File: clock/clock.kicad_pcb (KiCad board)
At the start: 2 copper layers, 100 x 50 mm, 165 parts, among them J1 Conn_02x05_Odd_Even, P1 Conn_WallPlug, U1 74HC596, U10 74HC596, U11 LPC804-TSSOP24, U2 74HC596, U3 74HC596, U4 74HC596, U5 74HC596, U6 74HC596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

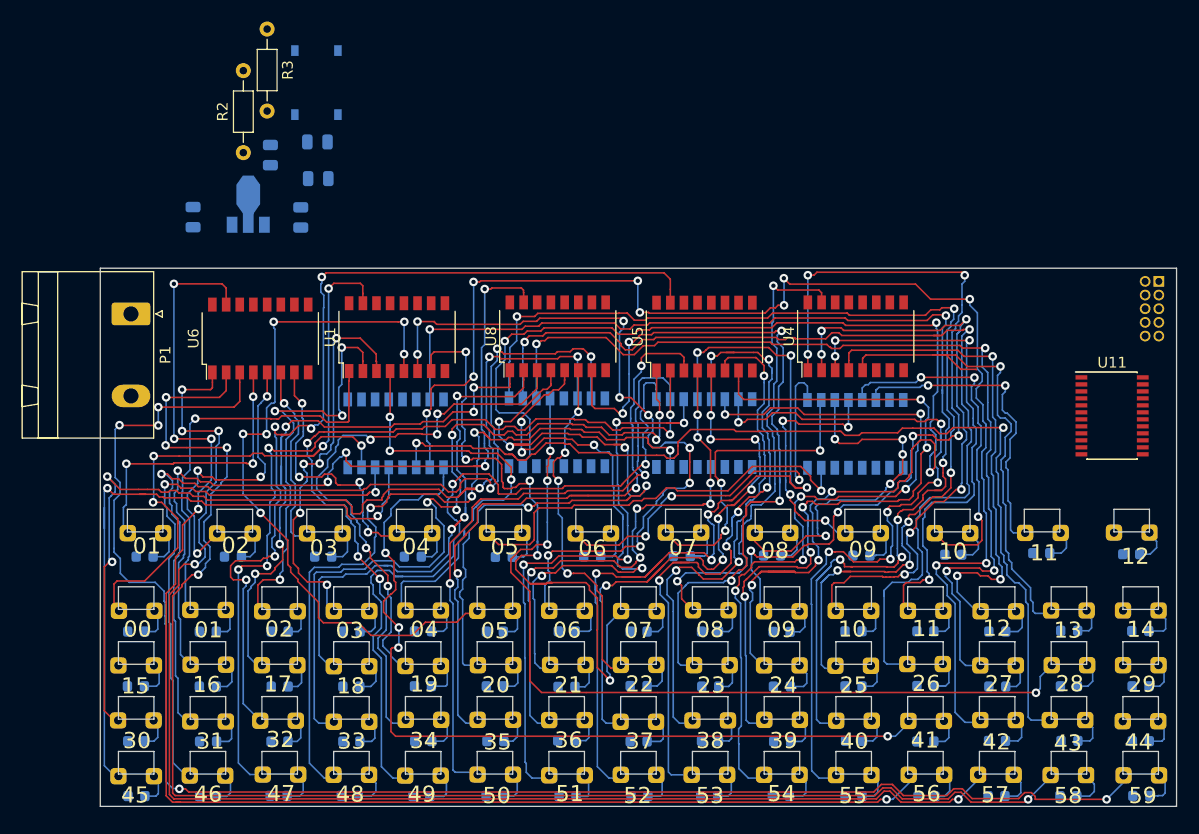
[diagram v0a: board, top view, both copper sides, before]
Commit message: All LEDs routed. Will consider some optimization e.g. via reduction or shorting traces.
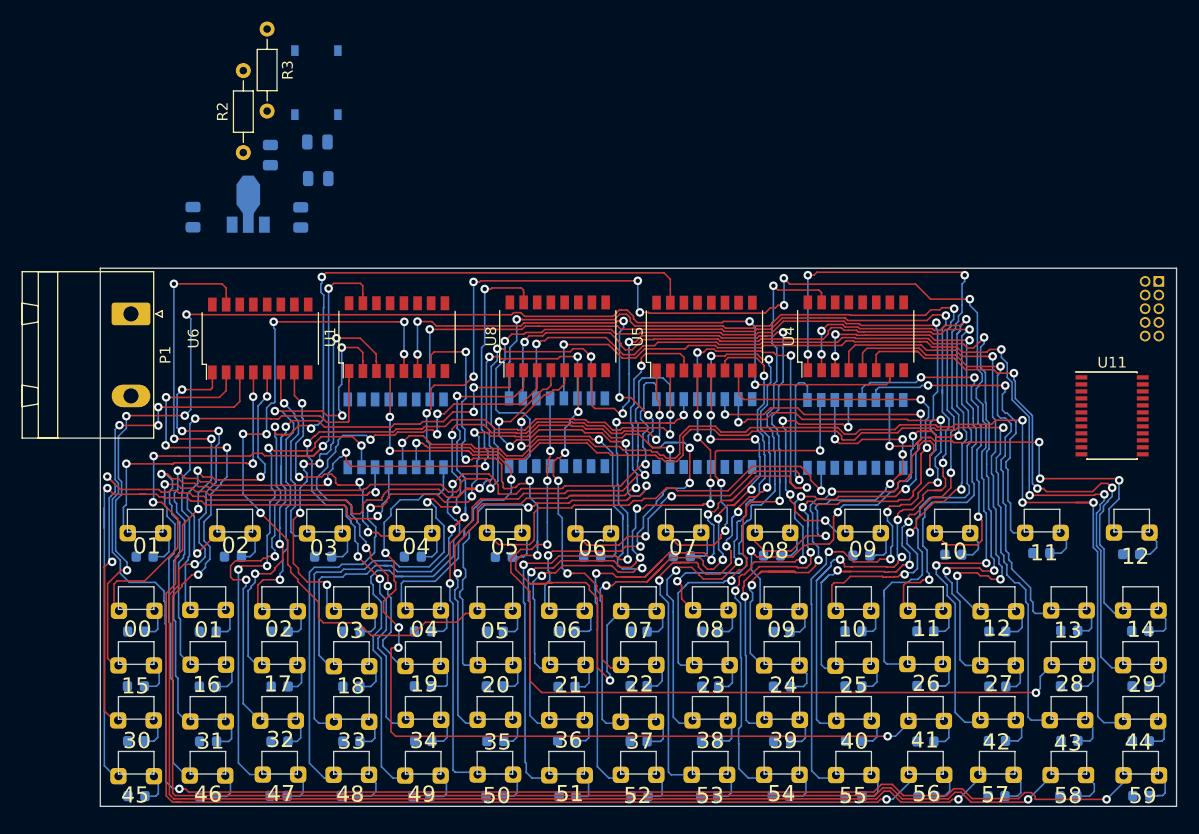
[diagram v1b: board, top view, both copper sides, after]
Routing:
- net M15: track 0.00 -> 114.5 mm, vias 0 -> 6
- net M44: track 0.00 -> 104.6 mm, vias 0 -> 4
- net M29: track 0.00 -> 87.3 mm, vias 0 -> 4
- net M14: track 0.00 -> 48.4 mm, vias 0 -> 3
- net H12: track 0.00 -> 36.1 mm, vias 0 -> 4
- net M13: track 46.3 -> 42.3 mm
- net M20: track 66.8 -> 64.5 mm
- net M27: track 85.4 -> 86.9 mm
- net M51: track 55.4 -> 54.0 mm
- net M53: track 68.7 -> 67.3 mm
- net M23: track 71.7 -> 72.7 mm
- net M48: track 72.4 -> 71.5 mm
- net M11: track 47.9 -> 48.8 mm
- net M21: track 53.8 -> 53.1 mm
- net M09: track 73.6 -> 74.3 mm

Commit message: Moving to a new work.
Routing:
- net M23: track 72.7 -> 75.4 mm
- net M24: track 116.4 -> 115.7 mm

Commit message: Added Renders
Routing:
- net M01: track 38.7 -> 45.7 mm
- net M24: track 115.7 -> 110.4 mm
- net M32: track 88.3 -> 84.9 mm
- net M30: track 91.9 -> 89.8 mm
- net M00: track 59.3 -> 60.8 mm
- net H12: track 36.1 -> 35.0 mm
- net M09: track 74.3 -> 73.2 mm
- net M25: track 97.0 -> 96.2 mm
- net M19: track 51.1 -> 50.4 mm
- net H02: track 28.2 -> 27.4 mm
- net M38: track 48.7 -> 48.1 mm
- net M43: track 93.0 -> 92.4 mm
- net M46: track 51.5 -> 50.9 mm
- net M45: track 61.8 -> 61.3 mm
- net M16: track 73.7 -> 73.1 mm
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
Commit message: saving progress
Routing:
- net M55: track 69.5 -> 68.0 mm
- net M40: track 110.9 -> 109.7 mm
- net M25: track 96.2 -> 95.2 mm
- net H11: track 29.0 -> 29.5 mm
- net M24: track 110.4 -> 109.9 mm

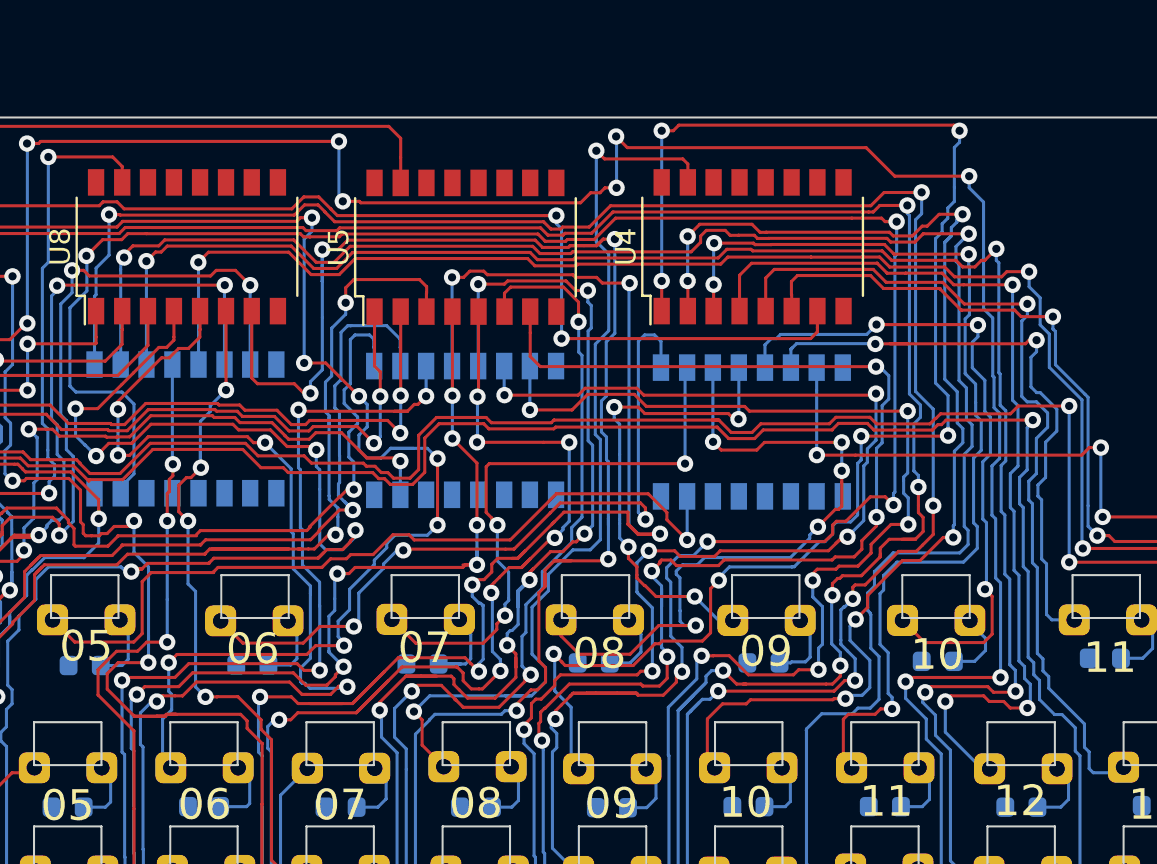
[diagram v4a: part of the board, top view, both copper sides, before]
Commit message: Completed LED castellated hole test board
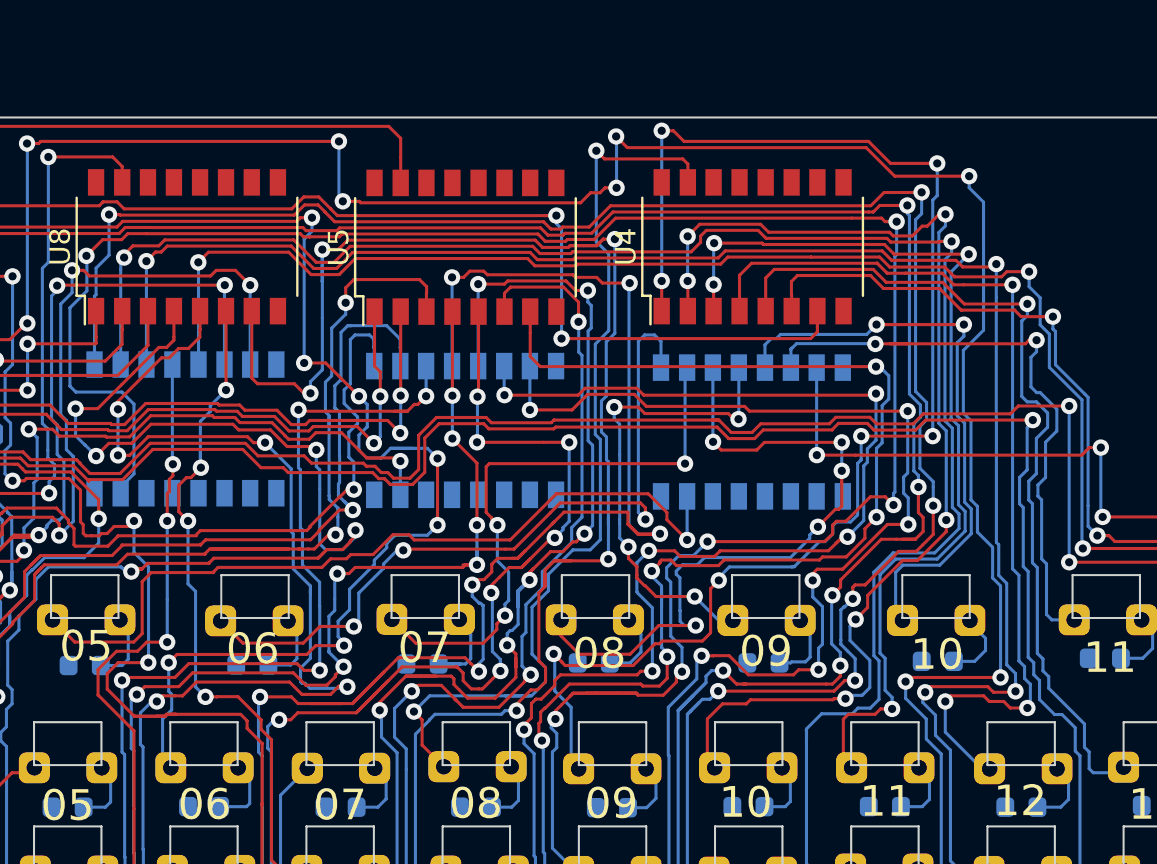
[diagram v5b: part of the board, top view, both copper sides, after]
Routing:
- net H10: track 32.9 -> 28.8 mm, vias 3 -> 2
- net M09: track 73.2 -> 69.6 mm
- net M26: track 90.0 -> 87.1 mm
- net M10: track 57.3 -> 54.4 mm
- net M27: track 86.3 -> 84.9 mm
- net M11: track 48.7 -> 47.7 mm
- net M40: track 109.7 -> 109.1 mm

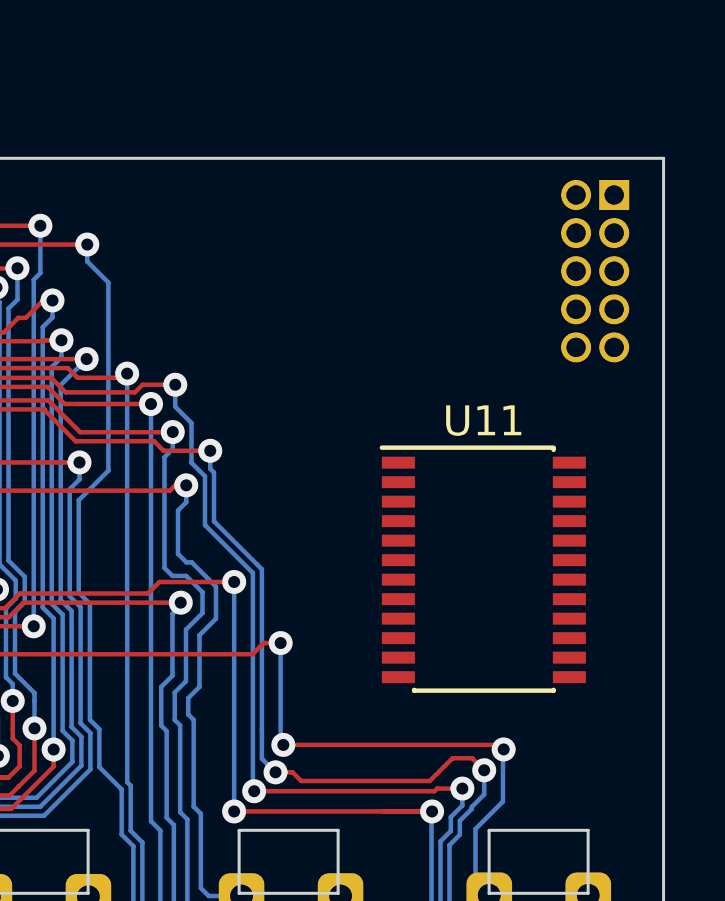
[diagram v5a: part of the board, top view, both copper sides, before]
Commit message: Converted the process from LPC804 to PIC18F45K20 due to time constraints.
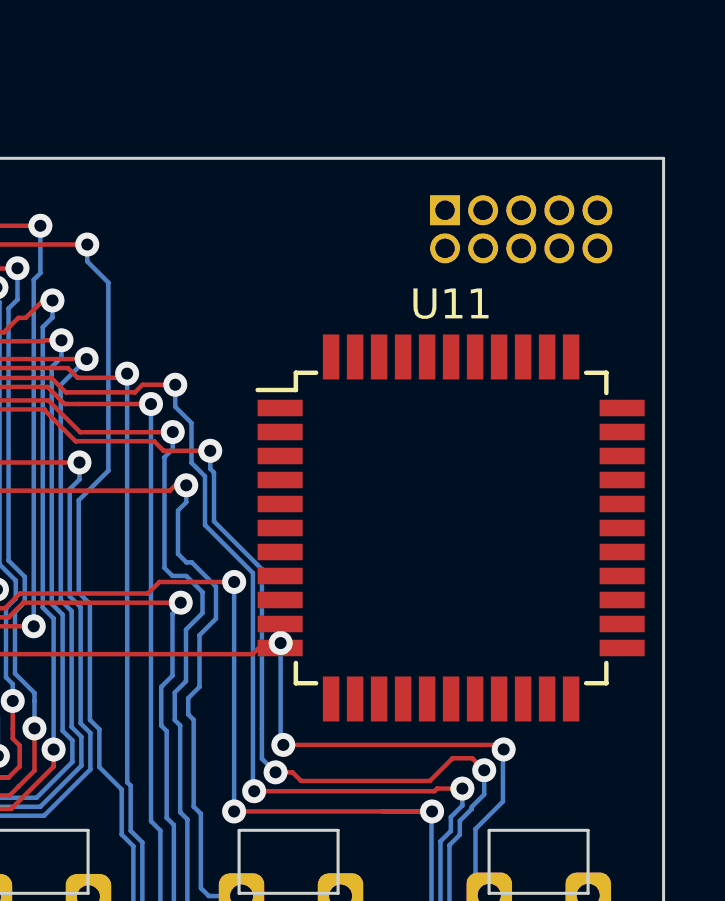
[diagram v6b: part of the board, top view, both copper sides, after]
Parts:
- U11: value LPC804-TSSOP24 -> PIC18F45K20_44-PIN_TQFP; footprint Package_SO:TSSOP-24_4.4x7.8mm_P0.65mm -> Package_QFP:TQFP-44_10x10mm_P0.8mm
- moved J1 5.66 mm to (130.0, 85.9), turned to 270 degrees
- moved U11 1.77 mm to (130.2, 96.5)
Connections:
- U11 pad 1: SD3 -> Net-(U11-Pad1)
- U11 pad 10: OCS -> Net-(U11-Pad10)
- U11 pad 12: SD0 -> Net-(U11-Pad12)
- U11 pad 13: SD1 -> Net-(U11-Pad13)
- U11 pad 14: SD6 -> Net-(U11-Pad14)
- U11 pad 18: 3v3 -> Net-(U11-Pad18)
- U11 pad 19: GND -> Net-(U11-Pad19)
- U11 pad 2: SD5 -> SD4
- U11 pad 22: ~CLR -> Net-(U11-Pad22)
- U11 pad 23: SD7 -> Net-(U11-Pad23)
- U11 pad 24: SD2 -> Net-(U11-Pad24)
- U11 pad 3: SD4 -> SD5
- U11 pad 4: SD8 -> SD6
- U11 pad 5: LCS -> SD7
- U11 pad 6: ~RST -> GND
- U11 pad 7: Net-(U11-Pad7) -> 3v3
- U11 pad 8: SWCLK -> Net-(U11-Pad8)
- U11 pad 9: SWDIO -> Net-(U11-Pad9)

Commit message: Updated todo list and some tracing
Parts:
- added C4: 0.1uF, Capacitor_SMD:C_0805_2012Metric, F.Cu at (131.3, 89.4)
- added C5: 0.1uF, Capacitor_SMD:C_0805_2012Metric, F.Cu at (126.9, 89.4)
- added R1: 10K, Resistor_SMD:R_0805_2012Metric, F.Cu at (122.0, 89.4)
- J1: value Conn_02x05_Odd_Even -> Conn_01x06_Female; footprint Connector_PinHeader_1.27mm:PinHeader_2x05_P1.27mm_Vertical -> Connector_PinHeader_2.54mm:PinHeader_1x06_P2.54mm_Vertical
- moved J1 7.32 mm to (122.7, 86.2)
- moved U11 0.77 mm to (129.8, 97.1), turned to 90 degrees
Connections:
- J1 pad 1: 3v3 -> Vpp
- J1 pad 2: SWDIO -> 3v3
- J1 pad 4: SWCLK -> PGD
- J1 pad 5: GND -> PGC
- J1 pad 6: Net-(J1-Pad6) -> PGM
- U11 pad 15: Net-(U11-Pad15) -> PGM
- U11 pad 16: Net-(U11-Pad16) -> PGC
- U11 pad 17: Net-(U11-Pad17) -> PGD
- U11 pad 18: Net-(U11-Pad18) -> Vpp
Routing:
- net ~OE: track 0.00 -> 104.6 mm, vias 0 -> 10
- net 3v3: track 0.00 -> 27.7 mm, vias 0 -> 1
- net GND: track 0.00 -> 27.6 mm
- net Vpp: track 0.00 -> 23.8 mm, vias 0 -> 1
- net PGD: track 0.00 -> 15.0 mm, vias 0 -> 1
- net PGM: track 0.00 -> 14.7 mm, vias 0 -> 1
- net PGC: track 0.00 -> 14.3 mm, vias 0 -> 1
- net M44: track 104.5 -> 99.5 mm
- net H12: track 35.0 -> 30.2 mm, vias 4 -> 3
- net M33: track 73.0 -> 68.8 mm
- net M14: track 48.4 -> 44.3 mm
- net M29: track 87.2 -> 83.4 mm
- net M52: track 83.4 -> 80.9 mm
- net M43: track 92.5 -> 90.1 mm
- net H11: track 29.5 -> 27.6 mm
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
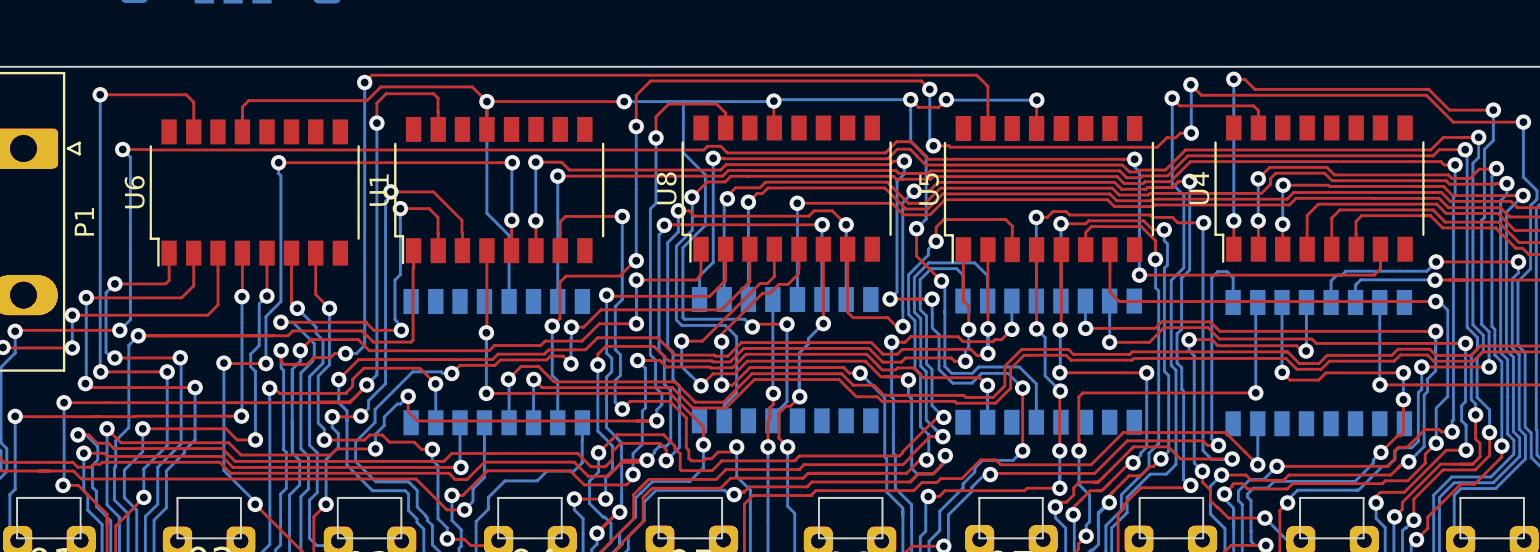
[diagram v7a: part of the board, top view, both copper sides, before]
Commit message: Verified the part selected for shift registers. The part is way off. Updated Schematic. Updating PCB lay out.
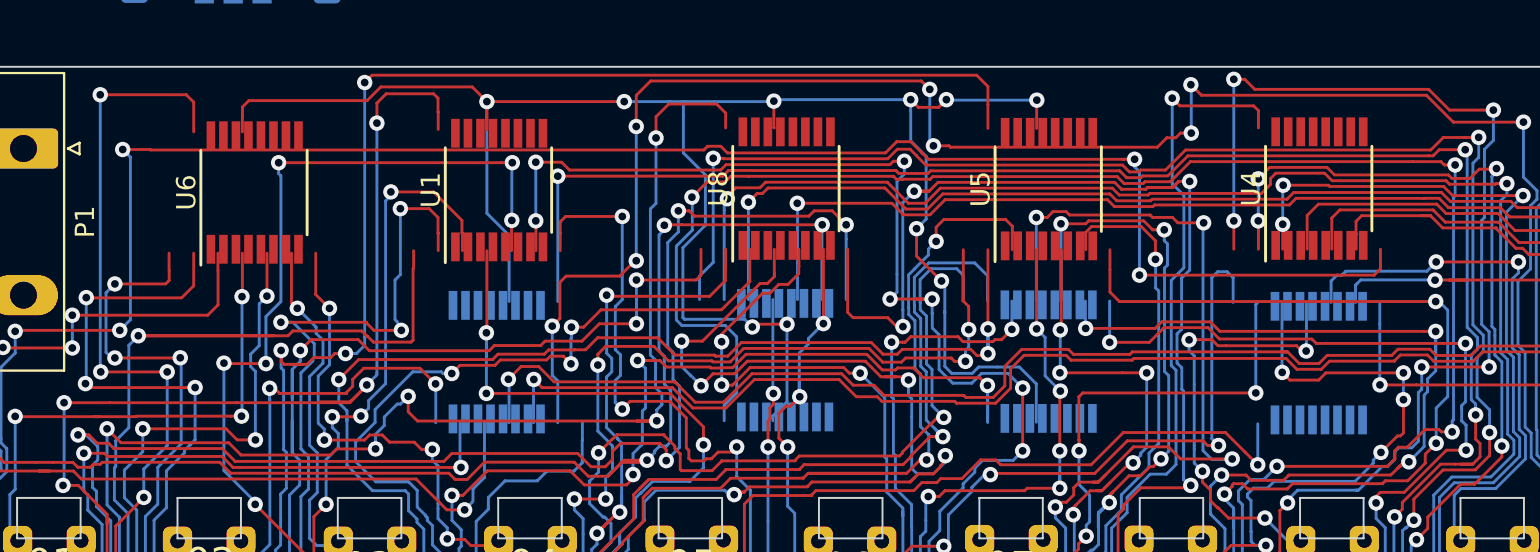
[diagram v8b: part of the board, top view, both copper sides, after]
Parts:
- U1, U10, U2, U3, U4, U5, U6, U8, U9: value 74HC596 -> NPIC6C596A; footprint Package_SO:SOP-16_4.4x10.4mm_P1.27mm -> Package_SO:TSSOP-16_4.4x5mm_P0.65mm
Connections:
- net Net-(D2-Pad1) renamed Power_Clk
- U1 pad 1: M01 -> 3v3
- U1 pad 10: OCS -> Net-(U1-Pad10)
- U1 pad 11: LSC -> M04
- U1 pad 12: Net-(U1-Pad12) -> M05
- U1 pad 13: ~OE -> M06
- U1 pad 14: SD0 -> M07
- U1 pad 15: M00 -> LSC
- U1 pad 16: Net-(U1-Pad16) -> GND
- U1 pad 2: M02 -> SD0
- U1 pad 3: M03 -> M00
- U1 pad 4: M04 -> M01
- U1 pad 5: M05 -> M02
- U1 pad 6: M06 -> M03
- U1 pad 7: M07 -> OCS
- U1 pad 8: GND -> ~OE
- U10 pad 1: H06 -> 3v3
- U10 pad 10: OCS -> Net-(U10-Pad10)
- U10 pad 11: LSC -> H09
- U10 pad 12: Net-(U10-Pad12) -> H10
- U10 pad 13: ~OE -> H11
- U10 pad 14: SD8 -> H12
- U10 pad 15: H05 -> LSC
- U10 pad 16: Net-(U10-Pad16) -> GND
- U10 pad 2: H07 -> SD8
- U10 pad 3: H08 -> H05
- U10 pad 4: H09 -> H06
- U10 pad 5: H10 -> H07
- U10 pad 6: H11 -> H08
- U10 pad 7: H12 -> OCS
- U10 pad 8: GND -> ~OE
- U2 pad 1: M25 -> 3v3
- U2 pad 10: OCS -> Net-(U2-Pad10)
- U2 pad 11: LSC -> M28
- U2 pad 12: Net-(U2-Pad12) -> M29
- U2 pad 13: ~OE -> M30
- U2 pad 14: SD3 -> M31
- U2 pad 15: M24 -> LSC
- U2 pad 16: Net-(U2-Pad16) -> GND
- U2 pad 2: M26 -> SD3
- U2 pad 3: M27 -> M24
- U2 pad 4: M28 -> M25
- U2 pad 5: M29 -> M26
- U2 pad 6: M30 -> M27
- U2 pad 7: M31 -> OCS
- U2 pad 8: GND -> ~OE
- U3 pad 1: M49 -> 3v3
- U3 pad 10: OCS -> Net-(U3-Pad10)
- U3 pad 11: LSC -> M52
- U3 pad 12: Net-(U3-Pad12) -> M53
- U3 pad 13: ~OE -> M54
- U3 pad 14: SD6 -> M55
- U3 pad 15: M48 -> LSC
- U3 pad 16: Net-(U3-Pad16) -> GND
- U3 pad 2: M50 -> SD6
- U3 pad 3: M51 -> M48
- U3 pad 4: M52 -> M49
- U3 pad 5: M53 -> M50
- U3 pad 6: M54 -> M51
- U3 pad 7: M55 -> OCS
- U3 pad 8: GND -> ~OE
- U4 pad 1: M09 -> 3v3
- U4 pad 10: OCS -> Net-(U4-Pad10)
- U4 pad 11: LSC -> M12
- U4 pad 12: Net-(U4-Pad12) -> M13
- U4 pad 13: ~OE -> M14
- U4 pad 14: SD1 -> M15
- U4 pad 15: M08 -> LSC
- U4 pad 16: Net-(U4-Pad16) -> GND
- U4 pad 2: M10 -> SD1
- U4 pad 3: M11 -> M08
- U4 pad 4: M12 -> M09
- U4 pad 5: M13 -> M10
- U4 pad 6: M14 -> M11
- U4 pad 7: M15 -> OCS
- U4 pad 8: GND -> ~OE
- U5 pad 1: M33 -> 3v3
- U5 pad 10: OCS -> Net-(U5-Pad10)
- U5 pad 11: LSC -> M36
- U5 pad 12: Net-(U5-Pad12) -> M37
- U5 pad 13: ~OE -> M38
- U5 pad 14: SD4 -> M39
- U5 pad 15: M32 -> LSC
- U5 pad 16: Net-(U5-Pad16) -> GND
- U5 pad 2: M34 -> SD4
- U5 pad 3: M35 -> M32
- U5 pad 4: M36 -> M33
- U5 pad 5: M37 -> M34
- U5 pad 6: M38 -> M35
- U5 pad 7: M39 -> OCS
- U5 pad 8: GND -> ~OE
- U6 pad 1: M57 -> 3v3
- U6 pad 10: OCS -> Net-(U6-Pad10)
- U6 pad 11: LSC -> H01
- U6 pad 12: Net-(U6-Pad12) -> H02
- U6 pad 13: ~OE -> H03
- U6 pad 14: SD7 -> H04
- U6 pad 15: M56 -> LSC
- U6 pad 16: Net-(U6-Pad16) -> GND
- U6 pad 2: M58 -> SD7
- U6 pad 3: M59 -> M56
- U6 pad 4: H01 -> M57
- U6 pad 5: H02 -> M58
- U6 pad 6: H03 -> M59
- U6 pad 7: H04 -> OCS
- U6 pad 8: GND -> ~OE
- U8 pad 1: M17 -> 3v3
- U8 pad 10: OCS -> Net-(U8-Pad10)
- U8 pad 11: LSC -> M23
- U8 pad 12: Net-(U8-Pad12) -> M22
- U8 pad 13: ~OE -> M21
- U8 pad 14: SD2 -> M20
- U8 pad 15: M16 -> LSC
- U8 pad 16: Net-(U8-Pad16) -> GND
- U8 pad 2: M18 -> SD2
- U8 pad 3: M19 -> M16
- U8 pad 4: M20 -> M17
- U8 pad 5: M21 -> M18
- U8 pad 6: M22 -> M19
- U8 pad 7: M23 -> OCS
- U8 pad 8: GND -> ~OE
- U9 pad 1: M41 -> 3v3
- U9 pad 10: OCS -> Net-(U9-Pad10)
- U9 pad 11: LSC -> M44
- U9 pad 12: Net-(U9-Pad12) -> M45
- U9 pad 13: ~OE -> M46
- U9 pad 14: SD5 -> M47
- U9 pad 15: M40 -> LSC
- U9 pad 16: Net-(U9-Pad16) -> GND
- U9 pad 2: M42 -> SD5
- U9 pad 3: M43 -> M40
- U9 pad 4: M44 -> M41
- U9 pad 5: M45 -> M42
- U9 pad 6: M46 -> M43
- U9 pad 7: M47 -> OCS
- U9 pad 8: GND -> ~OE
